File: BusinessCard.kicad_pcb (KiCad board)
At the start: 2 copper layers, 51 x 89 mm, 178 parts, among them J1 Conn_01x03_Socket, J2 Conn_01x04_Socket, J3 Conn_01x02, SW1 Up, SW2 Left, SW3 Down, SW4 Right, SW5 Toggle, SW6 Play/Pause, U1 STM32F103C8T6

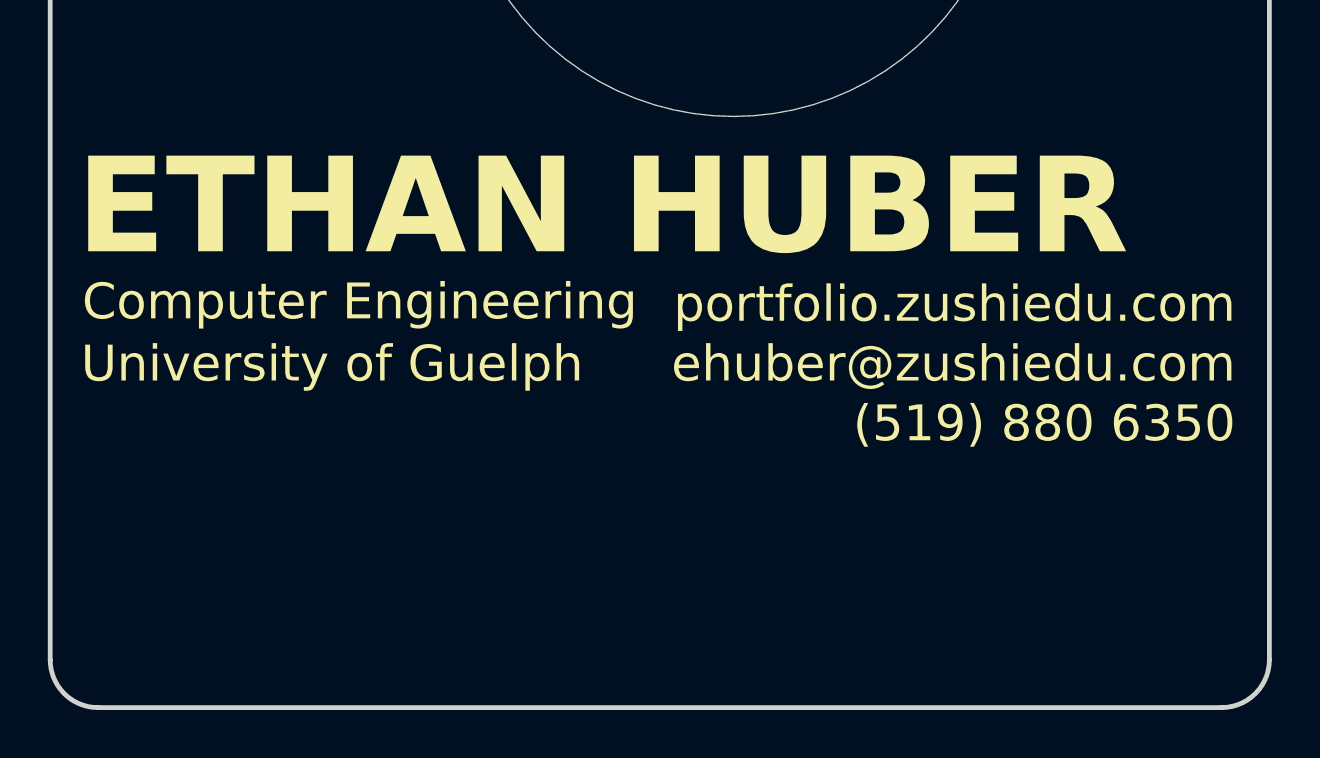
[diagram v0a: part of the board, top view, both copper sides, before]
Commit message: Add various SMD resistor footprints and mounting hole
Added new SMD resistor footprints (0201, 0402, 0805, 2010, 2512) and a 3.2mm M3 mounting hole to the PCB layout. Updated backup files and removed an old autosave.
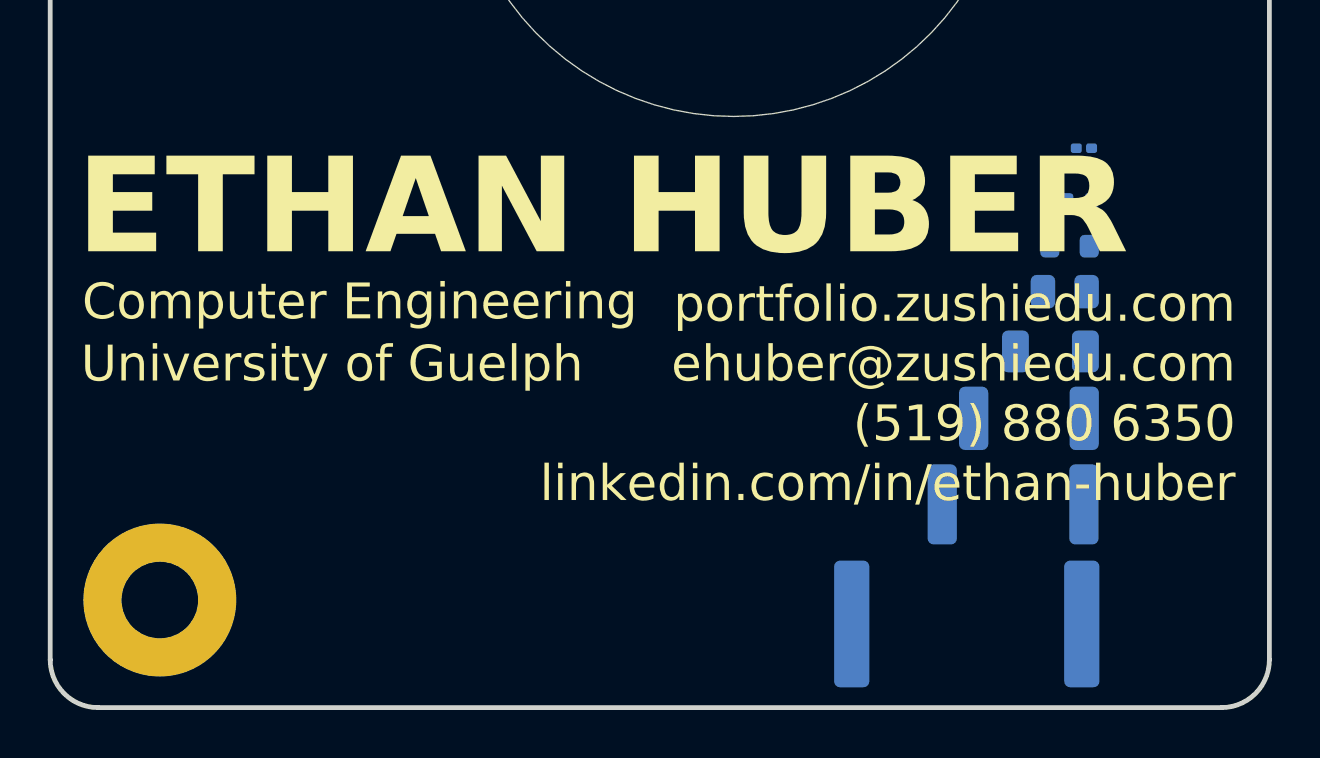
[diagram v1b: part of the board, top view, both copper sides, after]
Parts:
- added REF**: MountingHole_3.2mm_M3_Pad, MountingHole:MountingHole_3.2mm_M3_Pad, F.Cu at (139.5, 132.5)
- added REF**: R_0201_0603Metric, Resistor_SMD:R_0201_0603Metric, B.Cu at (178.2, 113.6)
- added REF**: R_2010_5025Metric, Resistor_SMD:R_2010_5025Metric, B.Cu at (175.9, 124.9)
- added REF**: R_0402_1005Metric, Resistor_SMD:R_0402_1005Metric, B.Cu at (178.0, 115.8)
- added REF**: R_0805_2012Metric, Resistor_SMD:R_0805_2012Metric, B.Cu at (177.4, 119.6)
- added REF**: R_2512_6332Metric, Resistor_SMD:R_2512_6332Metric, B.Cu at (175.2, 128.5)
- added REF**: R_4020_10251Metric, Resistor_SMD:R_4020_10251Metric, B.Cu at (173.3, 133.5)
- added REF**: R_1206_3216Metric, Resistor_SMD:R_1206_3216Metric, B.Cu at (176.8, 122.1)
- added REF**: R_0603_1608Metric, Resistor_SMD:R_0603_1608Metric, B.Cu at (177.6, 117.7)
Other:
- board text added: "0 1 2 3 4 5 6 7 8 9"
- board text added: "0201"
- board text added: "0402"
- board text added: "0603"
- board text added: "0805"
- board text added: "1 10 100 1K 10K 100K 1M 10M 100M 1G"
- board text added: "1206"
- board text added: "2010"
- board text added: "2512"
- board text added: "4020"
- board text added: "Black Brown Red Orange Yellow Green Blue Violet Grey White"
- board text added: "Passive(imp)"
- board text added: "Resistors(Ω)"
- board text added: "det(λI-A)=0"
- board text added: "linkedin.com/in/ethan-huber"
- board text removed: "80"

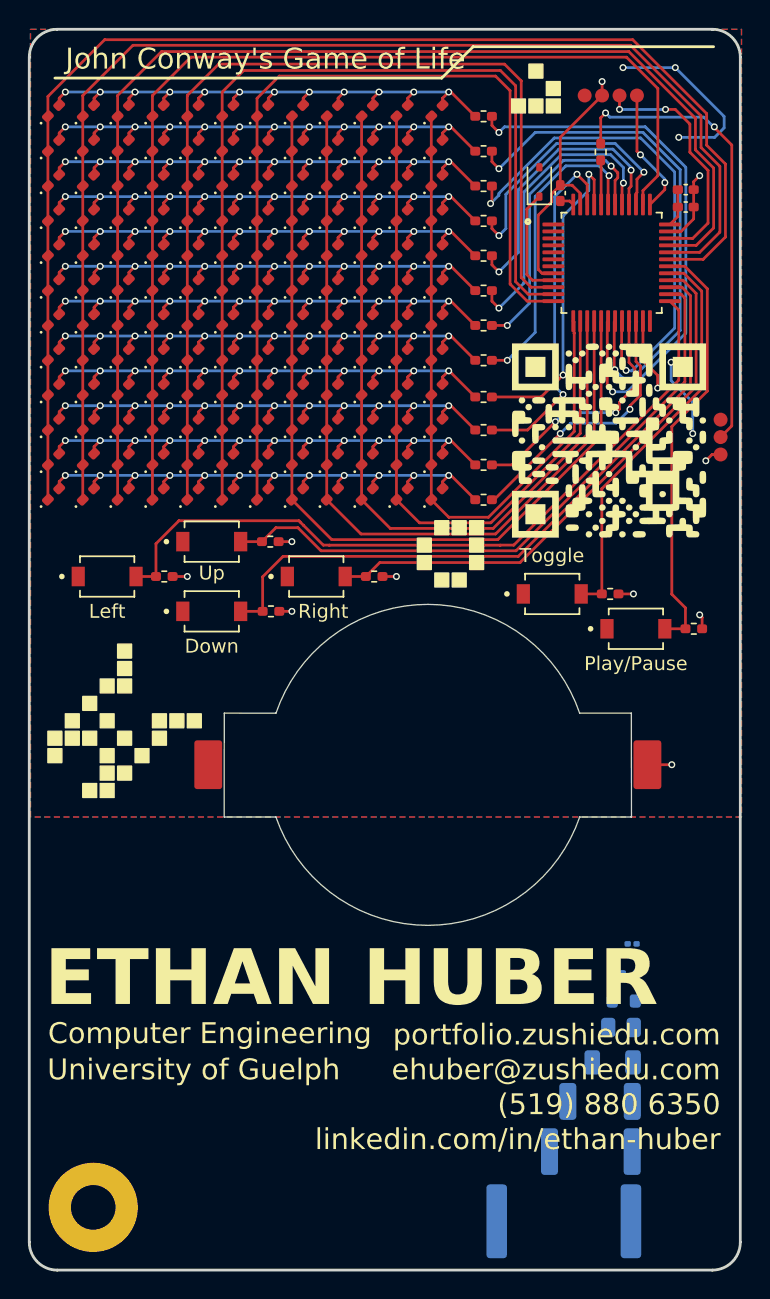
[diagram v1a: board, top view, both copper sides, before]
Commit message: Add logo footprint and update TQFP-32 package
Added a new 'LOGO' footprint to the front copper layer and replaced the 'R_0201_0603Metric' resistor footprint with a 'TQFP-32_7x7mm_P0.8mm' package on the back copper layer. Updated backup files and made minor adjustments to mounting hole and property attributes.
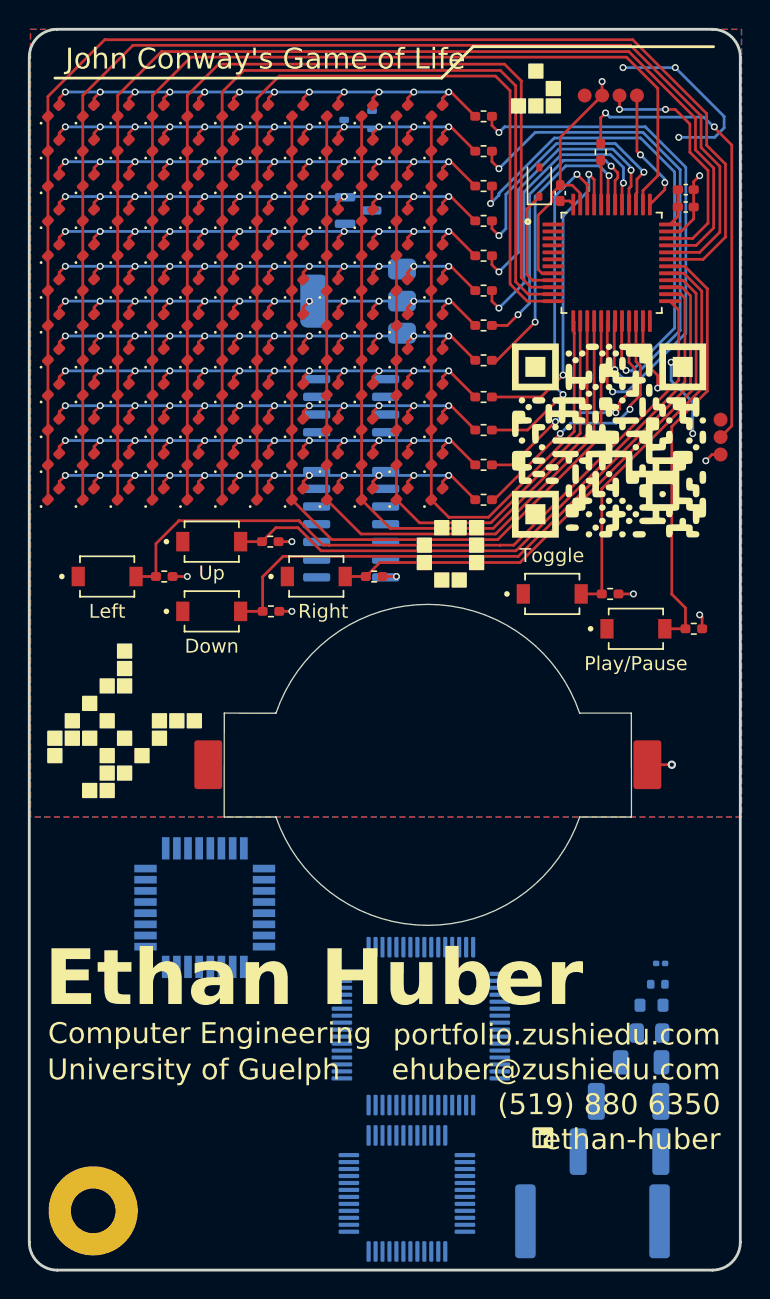
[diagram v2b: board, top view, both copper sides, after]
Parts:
- added G***: LOGO, LOGO, F.Cu at (171.8, 127.5)
- added G***: LOGO, LOGO, B.Cu at (150.5, 73.0)
- added G***: LOGO, LOGO, B.Cu at (182.0, 101.5)
- added G***: LOGO, LOGO, B.Cu at (182.0, 94.5)
- added G***: LOGO, LOGO, B.Cu at (179.5, 108.0)
- added REF**: SOT-23, Package_TO_SOT_SMD:SOT-23, B.Cu at (158.5, 61.0)
- added REF**: SOIC-14_3.9x8.7mm_P1.27mm, Package_SO:SOIC-14_3.9x8.7mm_P1.27mm, B.Cu at (158.0, 83.5)
- added REF**: TQFP-48_7x7mm_P0.5mm, Package_QFP:TQFP-48_7x7mm_P0.5mm, B.Cu at (162.0, 131.5)
- added REF**: TQFP-32_7x7mm_P0.8mm, Package_QFP:TQFP-32_7x7mm_P0.8mm, B.Cu at (147.5, 111.0)
- added REF**: TQFP-64_10x10mm_P0.5mm, Package_QFP:TQFP-64_10x10mm_P0.5mm, B.Cu at (163.0, 119.5)
- added REF**: SOIC-8_3.9x4.9mm_P1.27mm, Package_SO:SOIC-8_3.9x4.9mm_P1.27mm, B.Cu at (158.0, 75.0)
- added REF**: SOT-323_SC-70, Package_TO_SOT_SMD:SOT-323_SC-70, B.Cu at (158.5, 54.5)
- added REF**: SOT-223, Package_TO_SOT_SMD:SOT-223, B.Cu at (158.5, 67.5)
- moved REF** 2.48 mm to (180.2, 115.0)
- moved REF** 2.16 mm to (180.0, 116.5)
- moved REF** 2.08 mm to (179.4, 120.0)
- moved REF** 2.06 mm to (177.2, 128.5)
- moved REF** 2.06 mm to (175.3, 133.5)
- moved REF** 2.05 mm to (178.8, 122.1)
- moved REF** 2.05 mm to (177.9, 124.9)
- moved REF** 2.01 mm to (179.5, 118.0)
- moved REF** 0.25 mm to (139.5, 132.8)
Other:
- board text added: "+"
- board text added: "-"
- board text added: "A"
- board text added: "C"
- board text added: "Constants"
- board text added: "Conversions"
- board text added: "Ethan Huber"
- board text added: "M3"
- board text added: "NPN"
- board text added: "PNP"
- board text added: "SOIC14"
- board text added: "SOIC8"
- board text added: "SOT223"
- board text added: "SOT23"
- board text added: "SOT323"
- board text added: "TQFP32 0.8mm"
- board text added: "TQFP48 0.5mm"
- board text added: "TQFP64 0.5mm"
- board text added: "cm=inch x 2.54 km=mile x 1.609 m=feet x 0.3048 kg=lb x 0.454 kg=slug x 14.5939 L=Gal x 3.785 °C=(°F-32) x 5/9 °C=K-273.15"
- board text added: "e=1.602E-19 C k=8.99E9 Nm^2/C^2 c=299,792,458 m/s h=6.6260E-34 Js e=2.7182818284 π=3.1415926535 ϕ=1.6180339887"
- board text added: "ethan-huber"
- board text removed: "ETHAN HUBER"
- board text removed: "P(A|B)=P(A B)/P(B)"
- board text removed: "linkedin.com/in/ethan-huber"

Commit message: Rearranged back and added KiCad logo
- Rearranged back to avoid via collision
- Added KiCad logo
- Moved some via's for cleanliness
- Moved keychain hole label position
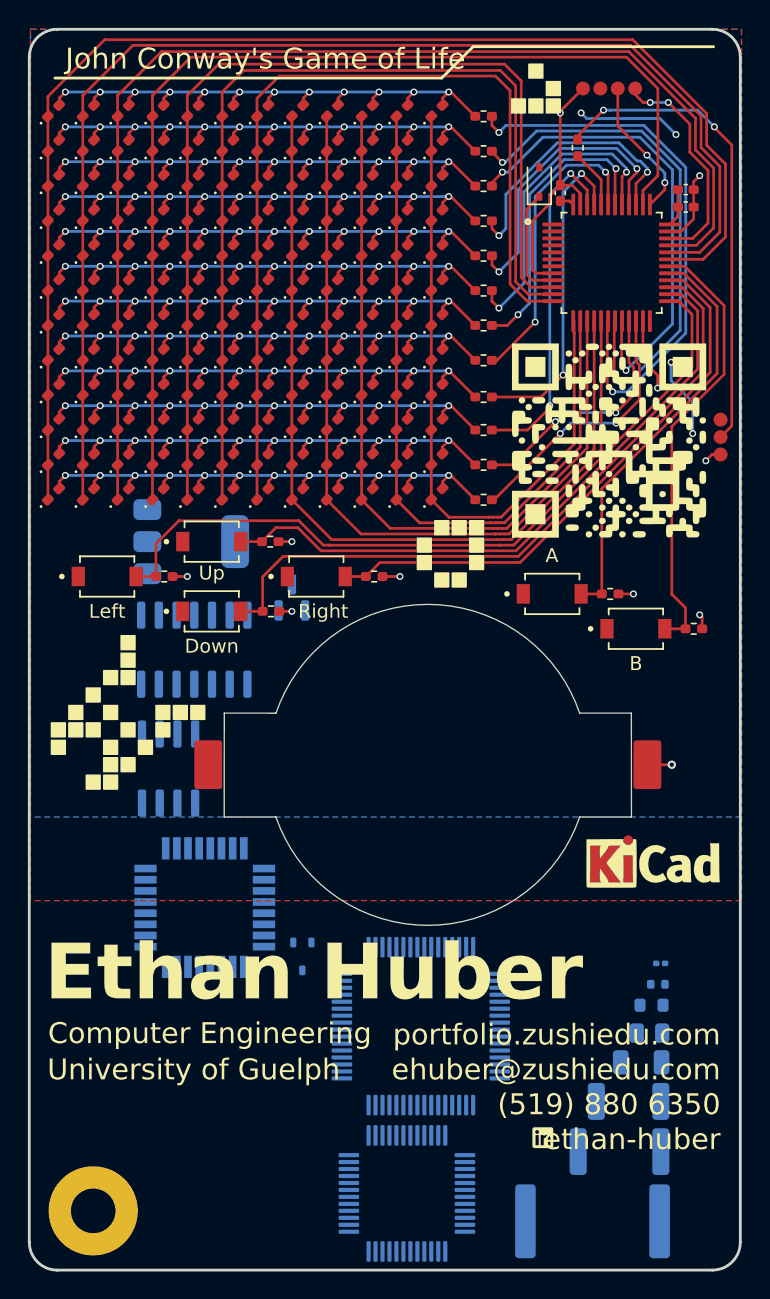
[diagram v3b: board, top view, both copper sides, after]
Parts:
- added G*** (x3): LOGO, LOGO, F.Cu at (179.6, 107.7)
- SW5: value Toggle -> A
- SW6: value Play/Pause -> B
- moved REF** 60.1 mm to (154.5, 114.5), turned to -90 degrees
- moved REF** 29.1 mm to (144.9, 101.0), turned to -90 degrees
- moved REF** 28.2 mm to (153.8, 88.8), turned to 90 degrees
- moved REF** 21.0 mm to (146.5, 84.8), turned to 0 degrees
- moved REF** 14.4 mm to (146.8, 92.5), turned to -90 degrees
- moved G*** 9.89 mm to (158.0, 66.5)
- moved J2 3.91 mm to (174.6, 52.2), turned to 0 degrees
- moved R1 1.68 mm to (174.2, 56.5)
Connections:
- J2 pad 1: Net-(J2-Pin_1) -> GND
- J2 pad 2: Net-(J2-Pin_2) -> +3.3V
- J2 pad 3: GND -> Net-(J2-Pin_3)
- J2 pad 4: +3.3V -> Net-(J2-Pin_4)
- U1 pad 34: Net-(J2-Pin_2) -> Net-(J2-Pin_4)
- U1 pad 37: Net-(J2-Pin_1) -> Net-(J2-Pin_3)
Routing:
- net Net-(J2-Pin_2): track 17.3 -> 0.00 mm, vias 2 -> 0
- net Net-(J2-Pin_4): track 0.00 -> 16.1 mm, vias 0 -> 2
- net Net-(J2-Pin_3): track 0.00 -> 10.2 mm, vias 0 -> 2
- net Net-(J2-Pin_1): track 9.09 -> 0.00 mm, vias 2 -> 0
- net +3.3V: track 22.6 -> 17.0 mm, vias 5 -> 4
- net R3: track 37.2 -> 35.0 mm
- net Left: track 53.5 -> 54.7 mm
- net B: track 30.7 -> 31.7 mm
- net Net-(U1-BOOT0): track 3.19 -> 4.17 mm
- net A: track 29.0 -> 29.9 mm
- net Right: track 39.8 -> 40.6 mm
- net Net-(J1-Pin_2): track 33.7 -> 34.4 mm
- net Up: track 45.2 -> 45.9 mm
- net Down: track 48.5 -> 49.3 mm
- net R5: track 20.4 -> 21.0 mm
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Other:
- board text added: "2"
- board text added: "e=1.602E-19 C k=8.99E9 Nm /C c=299,792,458 m/s h=6.6260E-34 Js e=2.7182818284 π=3.1415926535 ϕ=1.6180339887"
- board text removed: "e=1.602E-19 C k=8.99E9 Nm^2/C^2 c=299,792,458 m/s h=6.6260E-34 Js e=2.7182818284 π=3.1415926535 ϕ=1.6180339887"
